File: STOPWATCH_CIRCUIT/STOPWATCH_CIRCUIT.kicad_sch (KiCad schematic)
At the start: 21 parts, among them SW1 SW_START, SW2 SW_STOP, SW3 SW_RESET, SW4 SW_SPDT, U1 74AHC595, U2 LTC-4627JD, U3 TC1017-xCT

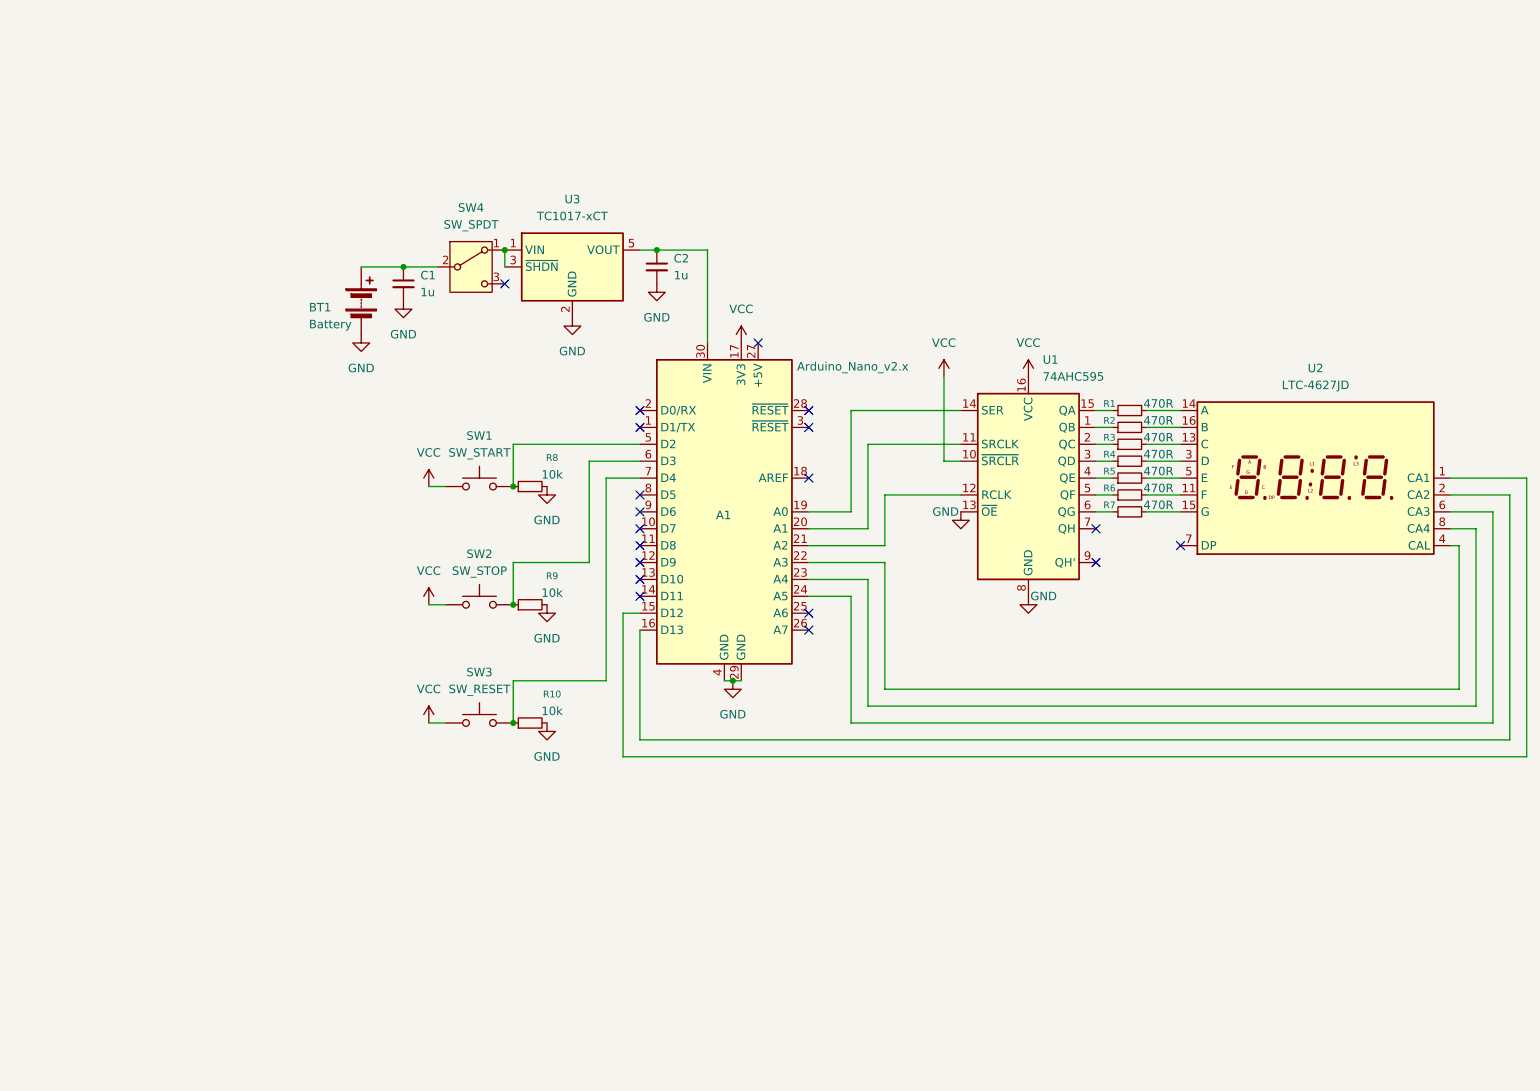
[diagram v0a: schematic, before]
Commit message: Finished adding the 2 extra digits for miliseconds and redid the whole board
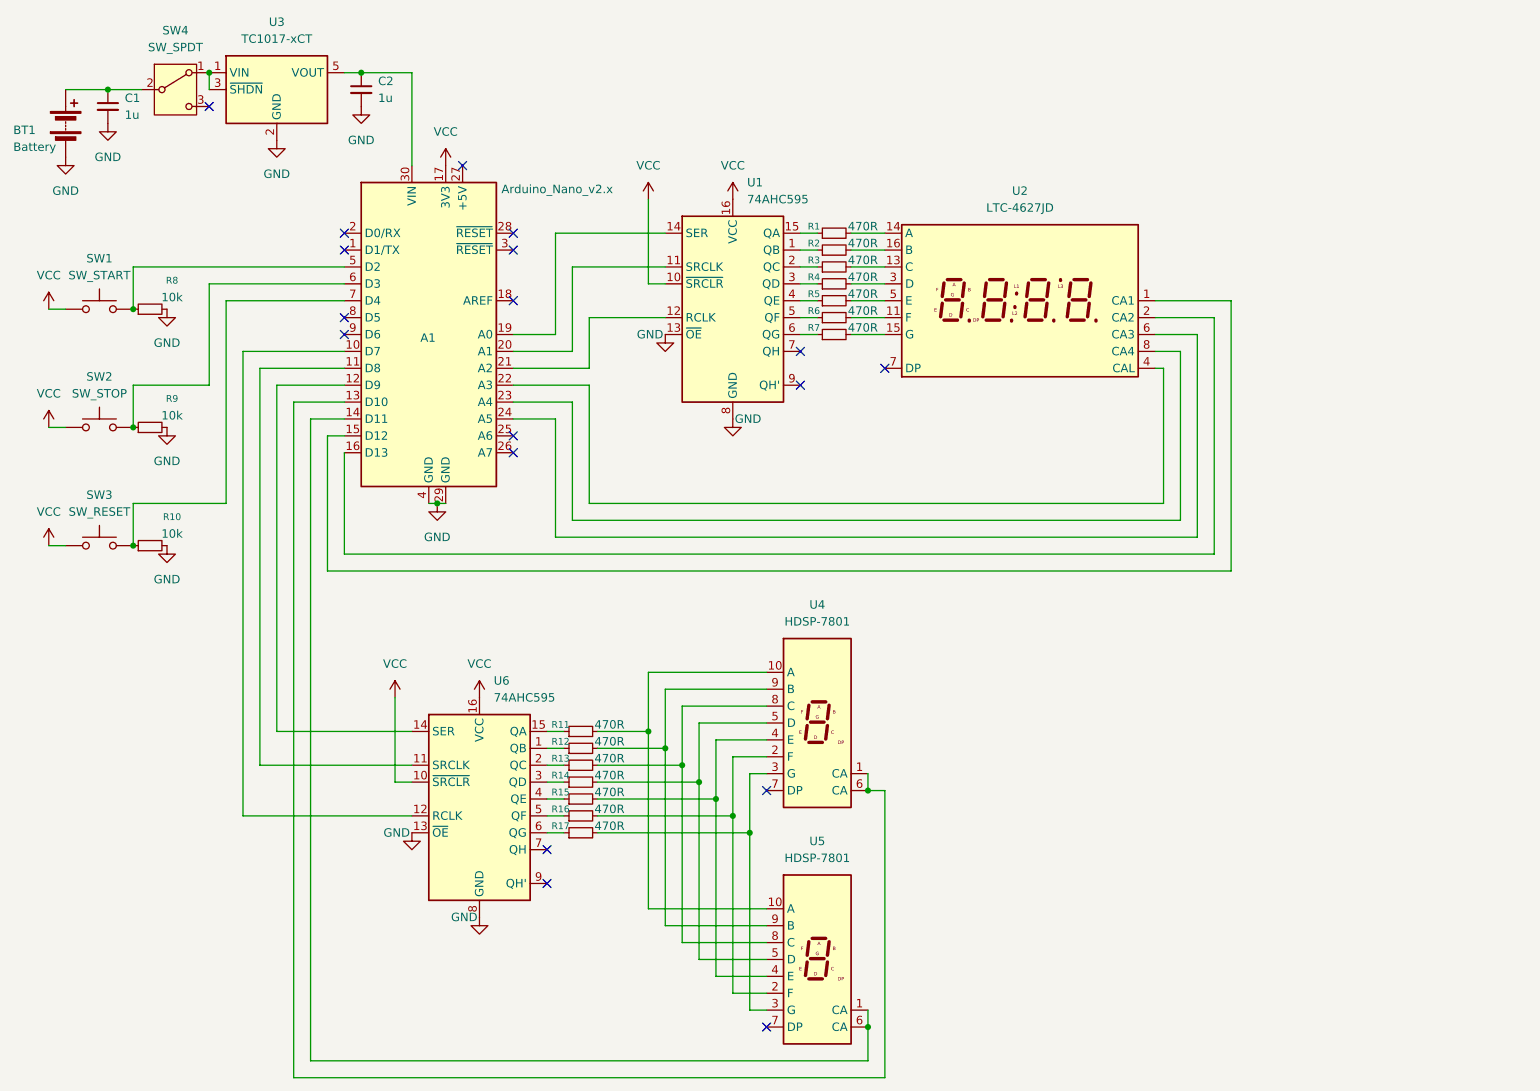
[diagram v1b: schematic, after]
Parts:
- added R11, R12, R13, R14, R15, R16, R17: 470R, Resistor_SMD:R_0805_2012Metric_Pad1.20x1.40mm_HandSolder, symbol Device:R_Small
- added U4, U5: HDSP-7801, Display_7Segment:HDSP-7801, symbol Display_Character:HDSP-7801
- added U6: 74AHC595, Package_SO:SOIC-16_3.9x9.9mm_P1.27mm, symbol 74xx:74AHC595
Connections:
- net GND: now also U6.13 (~{OE}), U6.8 (GND)
- net VCC: now also U6.10 (~{SRCLR}), U6.16 (VCC)
- net at A1.10 (D7): now also U6.12 (RCLK)
- net at A1.11 (D8): now also U6.11 (SRCLK)
- net at A1.12 (D9): now also U6.14 (SER)
- net at A1.13 (D10): now also U4.1 (CA), U4.6 (CA)
- net at A1.14 (D11): now also U5.1 (CA), U5.6 (CA)
- new net: R13.1, U6.2 (QC)
- new net: R13.2, U4.8 (C), U5.8 (C)
- new net: R14.1, U6.3 (QD)
- new net: R14.2, U4.5 (D), U5.5 (D)
- new net: R17.1, U6.6 (QG)
- new net: R17.2, U4.3 (G), U5.3 (G)
- new net: R11.2, U4.10 (A), U5.10 (A)
- new net: R16.2, U4.2 (F), U5.2 (F)
- new net: R15.2, U4.4 (E), U5.4 (E)
- new net: R12.2, U4.9 (B), U5.9 (B)
- new net: R12.1, U6.1 (QB)
- new net: R11.1, U6.15 (QA)
- new net: R15.1, U6.4 (QE)
- new net: R16.1, U6.5 (QF)
- no-connect marks 19 -> 18
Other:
- moved on the sheet: A1, BT1, C1, C2, R1, R10, R2, R3, R4, R5, R6, R7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
